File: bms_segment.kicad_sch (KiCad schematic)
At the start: 103 parts, among them J1 Conn_02x09_Counter_Clockwise, J2 Conn_02x09_Counter_Clockwise, J5 Conn_01x04, J6 Conn_01x04, J7 Conn_01x06, SW1 SW_Push, U1 LMR516xx, U2 MAX14921, U3 ADuM1252, U4 STM32F103C8Tx, U5 MAX11163, U6 REF61xx

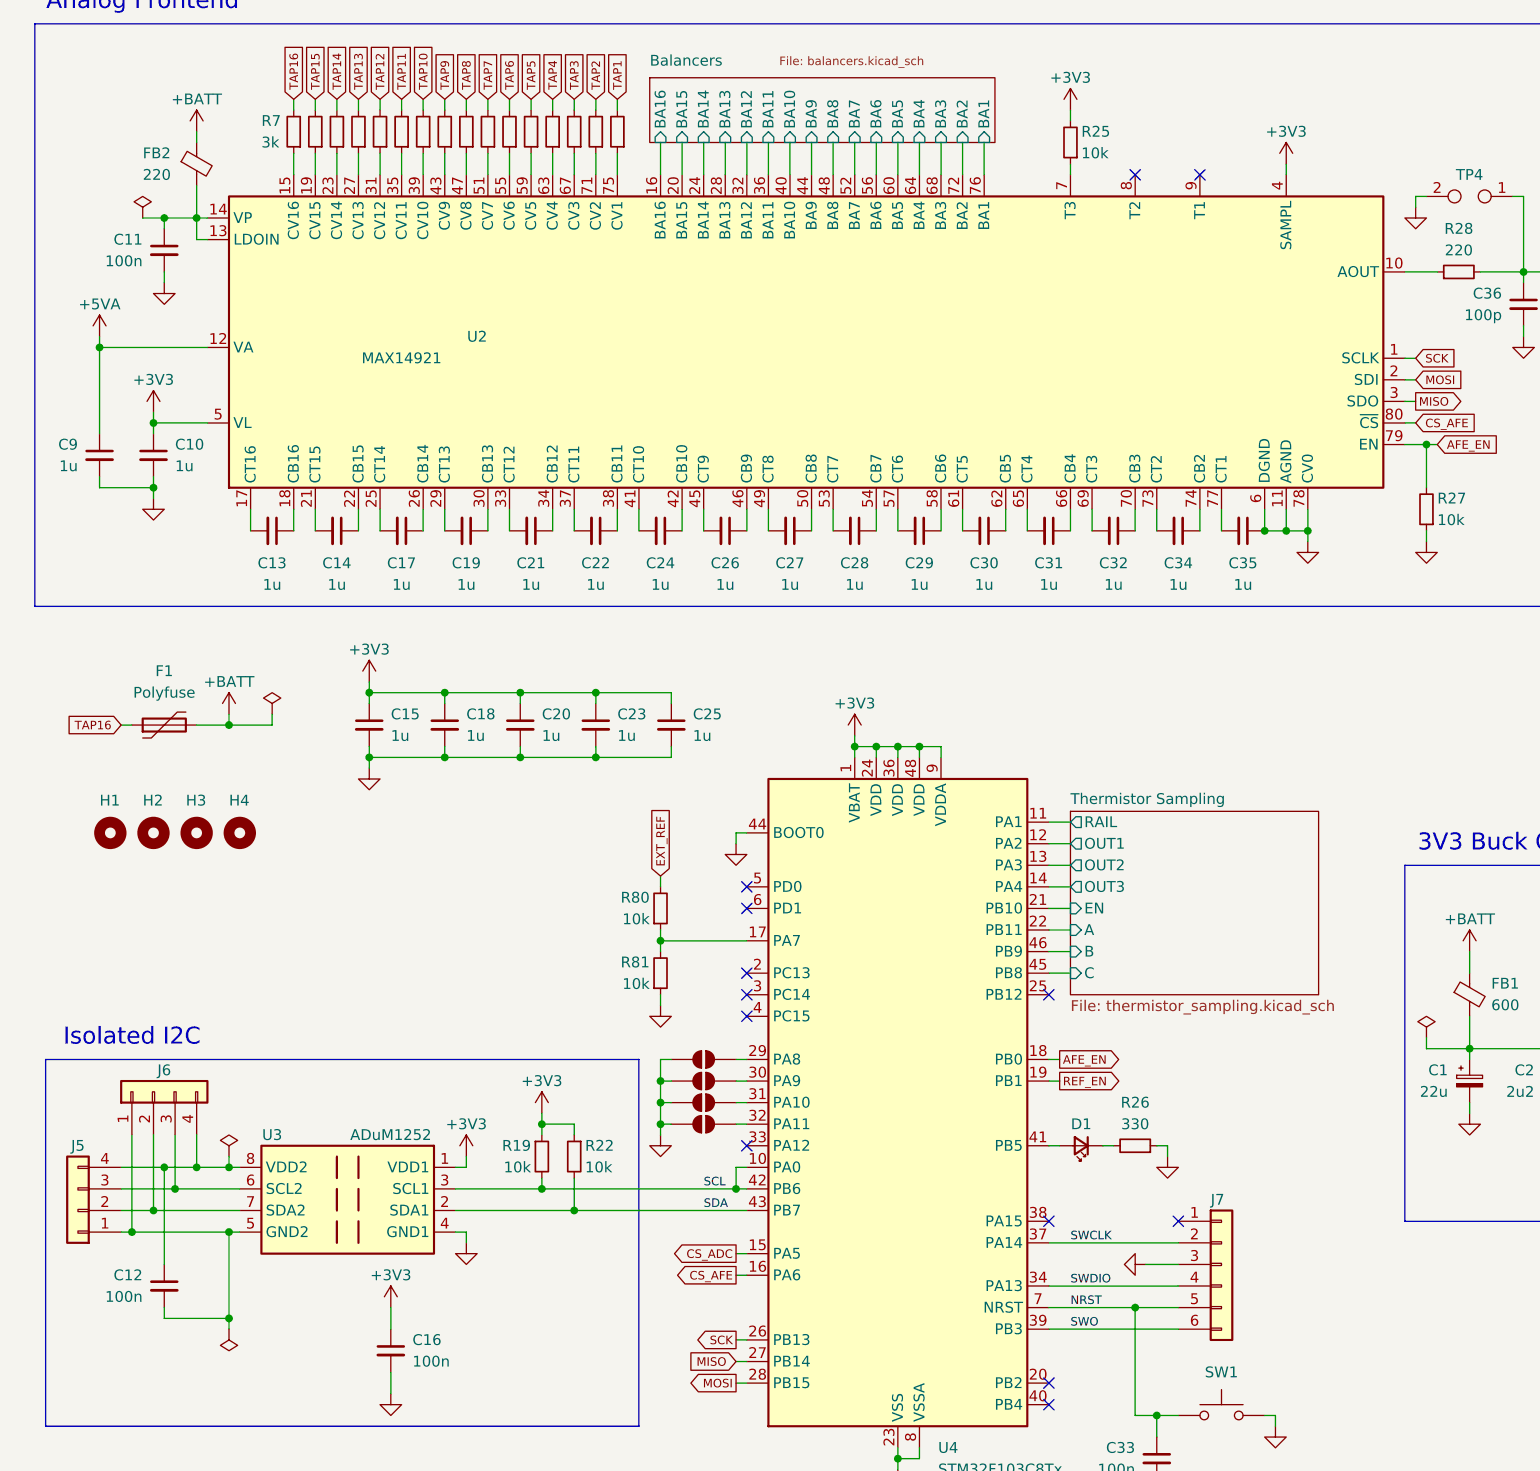
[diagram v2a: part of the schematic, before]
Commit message: schematic: Fix I2C connector pin order
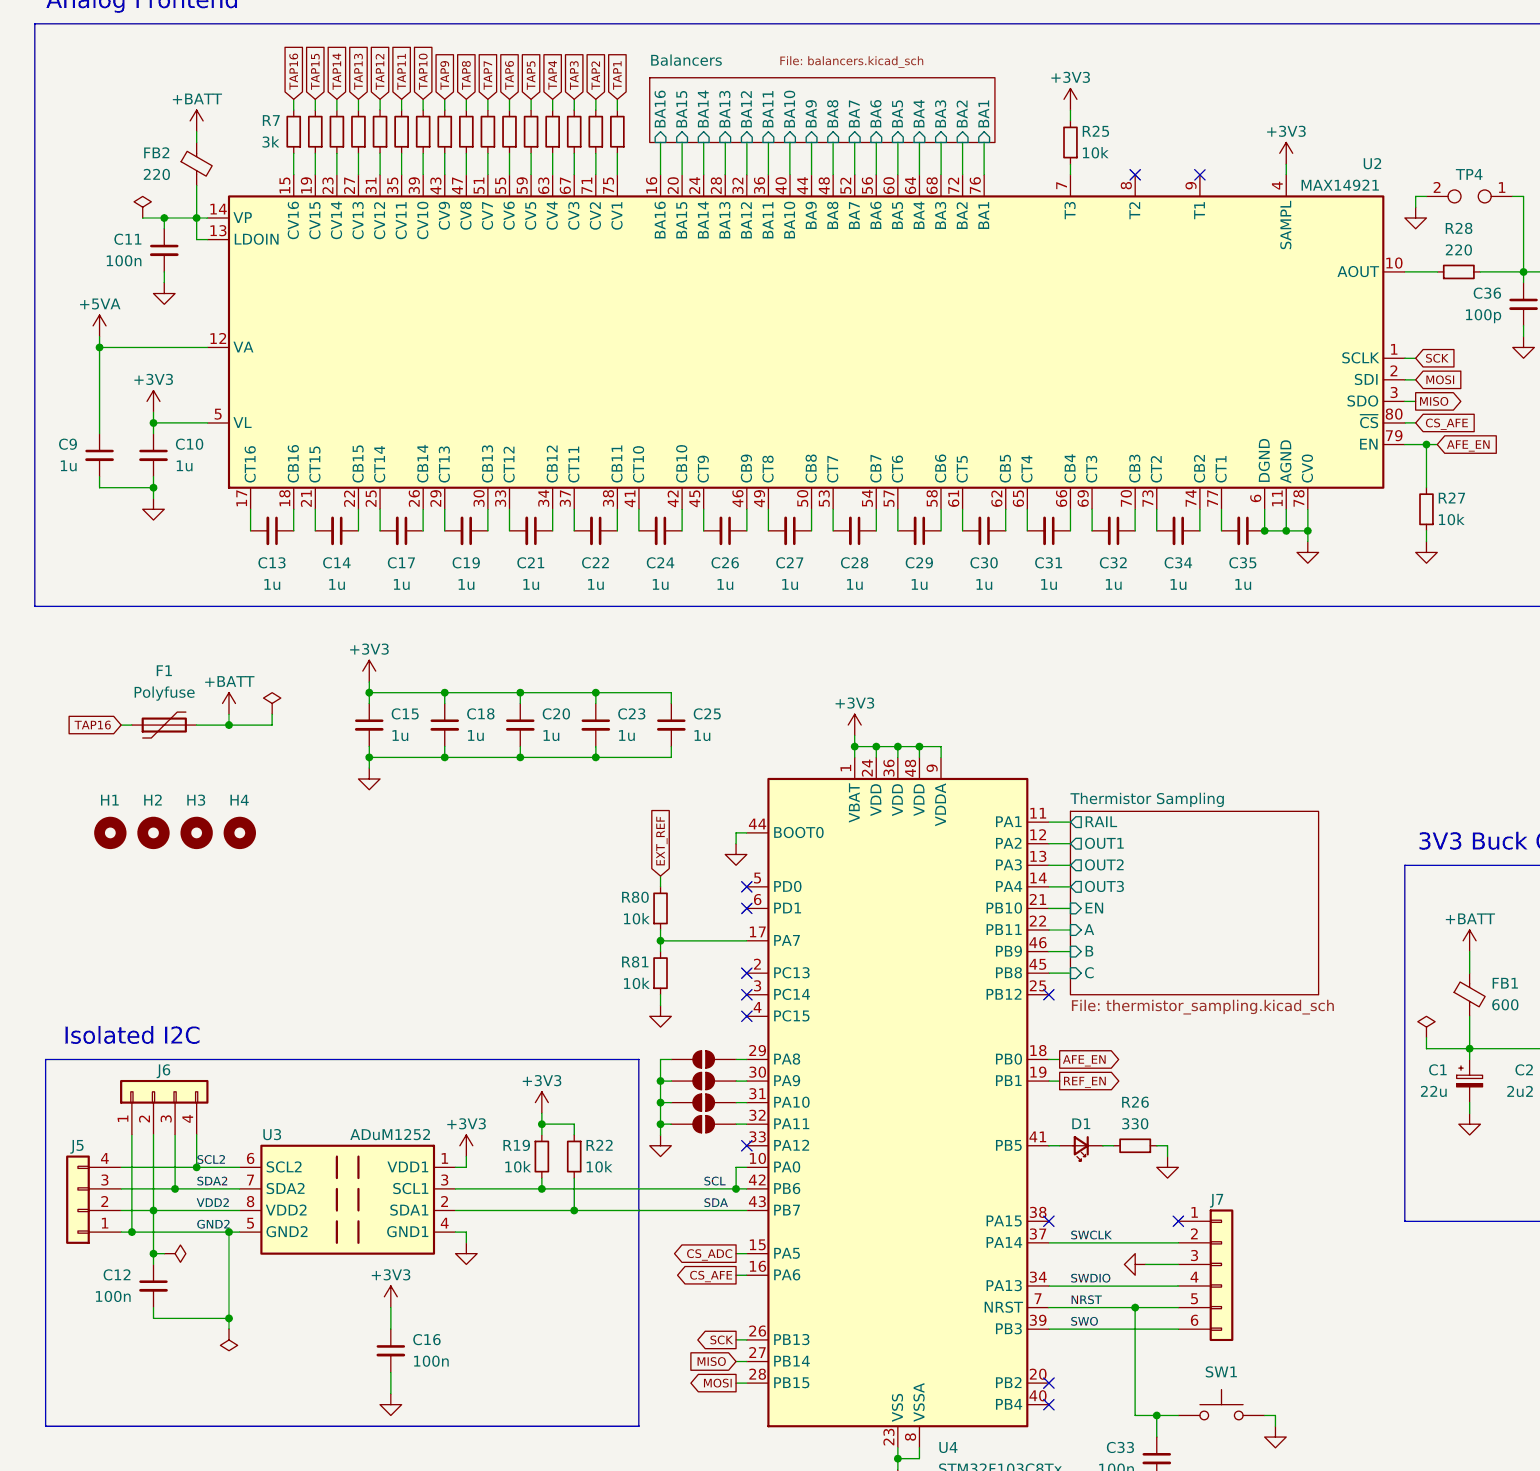
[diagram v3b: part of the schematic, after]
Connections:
- net GND2: now reaches C12.2, J5.1 (Pin_1), J6.1 (Pin_1), U3.5 (GND2)
- net SDA2: now reaches J5.3 (Pin_3), J6.3 (Pin_3)
- net SDA2: now also U3.7 (SDA2); no longer U3.6 (SCL2)
- net VDD2: now reaches J5.2 (Pin_2), J6.2 (Pin_2)
- net VDD2: now also C12.1, U3.8 (VDD2); no longer U3.7 (SDA2)
- net SCL2: now reaches J5.4 (Pin_4), J6.4 (Pin_4)
- net SCL2: now also U3.6 (SCL2); no longer C12.1, U3.8 (VDD2)
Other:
- moved on the sheet: C12
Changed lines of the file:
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@@
 	)
 	(junction
-		(at 30.48 153.67)
-		(diameter 0)
-		(color 0 0 0 0)
-	)
-	(junction
 		(at 74.93 148.59)
 		(diameter 0)
@@
 	)
 	(junction
-		(at 38.1 153.67)
-		(diameter 0)
-		(color 0 0 0 0)
-	)
-	(junction
 		(at 236.22 53.34)
 		(diameter 0)
@@
 	)
 	(junction
+		(at 29.21 163.83)
+		(diameter 0)
+		(color 0 0 0 0)
+	)
+	(junction
 		(at 240.03 29.21)
 		(diameter 0)
@@
 	(wire
 		(pts
-			(xy 29.21 158.75) (xy 39.37 158.75)
-		)
-		(stroke
-			(width 0)
-			(type default)
-		)
-	)
-	(wire
-		(pts
 			(xy 96.52 33.02) (xy 96.52 36.83)
 		)
@@
 	(wire
 		(pts
-			(xy 30.48 171.45) (xy 30.48 170.18)
-		)
-		(stroke
-			(width 0)
-			(type default)
-		)
-	)
-	(wire
-		(pts
-			(xy 25.4 153.67) (xy 30.48 153.67)
+			(xy 29.21 171.45) (xy 29.21 170.18)
 		)
 		(stroke
@@
 	(wire
 		(pts
+			(xy 29.21 158.75) (xy 39.37 158.75)
+		)
+		(stroke
+			(width 0)
+			(type default)
+		)
+	)
+	(wire
+		(pts
 			(xy 231.14 93.98) (xy 232.41 93.98)
 		)
@@
 	(wire
 		(pts
+			(xy 29.21 163.83) (xy 29.21 165.1)
+		)
+		(stroke
+			(width 0)
+			(type default)
+		)
+	)
+	(wire
+		(pts
 			(xy 231.14 99.06) (xy 231.14 101.6)
 		)
@@
 	(wire
 		(pts
+			(xy 29.21 163.83) (xy 30.48 163.83)
+		)
+		(stroke
+			(width 0)
+			(type default)
+		)
+	)
+	(wire
+		(pts
 			(xy 63.5 27.94) (xy 63.5 29.21)
 		)
@@
 	(wire
 		(pts
-			(xy 30.48 153.67) (xy 30.48 165.1)
-		)
-		(stroke
-			(width 0)
-			(type default)
-		)
-	)
-	(wire
-		(pts
 			(xy 255.27 147.32) (xy 255.27 148.59)
 		)
@@
 	(wire
 		(pts
-			(xy 38.1 153.67) (xy 39.37 153.67)
-		)
-		(stroke
-			(width 0)
-			(type default)
-		)
-	)
-	(wire
-		(pts
-			(xy 34.29 153.67) (xy 38.1 153.67)
+			(xy 34.29 153.67) (xy 39.37 153.67)
 		)
 		(stroke
@@
 	(wire
 		(pts
-			(xy 38.1 152.4) (xy 38.1 153.67)
-		)
-		(stroke
-			(width 0)
-			(type default)
-		)
-	)
-	(wire
-		(pts
 			(xy 261.62 101.6) (xy 262.89 101.6)
 		)
@@
 	(wire
 		(pts
-			(xy 30.48 153.67) (xy 34.29 153.67)
+			(xy 25.4 153.67) (xy 34.29 153.67)
 		)
 		(stroke
@@
 	(wire
 		(pts
-			(xy 30.48 171.45) (xy 38.1 171.45)
+			(xy 29.21 171.45) (xy 38.1 171.45)
 		)
 		(stroke
@@
 	(wire
 		(pts
+			(xy 29.21 158.75) (xy 29.21 163.83)
+		)
+		(stroke
+			(width 0)
+			(type default)
+		)
+	)
+	(wire
+		(pts
 			(xy 238.76 31.75) (xy 241.3 31.75)
 		)
@@
 		)
 	)
+	(label "GND2"
+		(at 34.29 161.29 0)
+		(effects
+			(font
+				(size 1 1)
+			)
+			(justify left bottom)
+		)
+	)
 	(label "NRST"
 		(at 137.16 170.18 0)
@@
 		)
 	)
+	(label "VDD2"
+		(at 34.29 158.75 0)
+		(effects
+			(font
+				(size 1 1)
+			)
+			(justify left bottom)
+		)
+	)
+	(label "SCL2"
+		(at 34.29 153.67 0)
+		(effects
+			(font
+				(size 1 1)
+			)
+			(justify left bottom)
+		)
+	)
+	(label "SDA2"
+		(at 34.29 156.21 0)
+		(effects
+			(font
+				(size 1 1)
+			)
+			(justify left bottom)
+		)
+	)
 	(label "SWO"
 		(at 137.16 172.72 0)
@@
 		(dnp no)
 		(property "Reference" "U2"
-			(at 67.31 55.88 90)
+			(at 172.72 35.56 90)
 			(effects
 				(font
@@
 		)
 		(property "Value" "MAX14921"
-			(at 58.42 58.42 90)
+			(at 168.91 38.1 90)
 			(effects
 				(font
@@
 	(symbol
 		(lib_id "Device:C_Small")
-		(at 30.48 167.64 0)
+		(at 29.21 167.64 0)
 		(mirror y)
 		(unit 1)
@@
 		(dnp no)
 		(property "Reference" "C12"
-			(at 27.94 166.3762 0)
+			(at 26.67 166.3762 0)
 			(effects
 				(font
@@
 		)
 		(property "Value" "100n"
-			(at 27.94 168.9162 0)
+			(at 26.67 168.9162 0)
 			(effects
 				(font
@@
 		)
 		(property "Footprint" "Capacitor_SMD:C_0603_1608Metric"
-			(at 30.48 167.64 0)
+			(at 29.21 167.64 0)
 			(effects
 				(font
@@
 		)
 		(property "Datasheet" "~"
-			(at 30.48 167.64 0)
+			(at 29.21 167.64 0)
 			(effects
 				(font
@@
 		)
 		(property "Description" "Unpolarized capacitor, small symbol"
-			(at 30.48 167.64 0)
+			(at 29.21 167.64 0)
 			(effects
 				(font
@@
 		)
 		(property "Dist #" "C1591"
-			(at 30.48 167.64 0)
+			(at 29.21 167.64 0)
 			(effects
 				(font
@@
 		)
 		(property "Mfr" "Samsung"
-			(at 30.48 167.64 0)
+			(at 29.21 167.64 0)
 			(effects
 				(font
@@
 		)
 		(property "Mfr #" "CL10B104KB8NNNC"
-			(at 30.48 167.64 0)
+			(at 29.21 167.64 0)
 			(effects
 				(font
@@
 		)
 		(property "Dist" "LCSC"
-			(at 30.48 167.64 0)
+			(at 29.21 167.64 0)
 			(effects
 				(font
@@
 	(symbol
 		(lib_id "power:PWR_FLAG")
-		(at 38.1 152.4 0)
+		(at 30.48 163.83 270)
 		(unit 1)
 		(exclude_from_sim no)
@@
 		(fields_autoplaced yes)
 		(property "Reference" "#FLG03"
-			(at 38.1 150.495 0)
+			(at 32.385 163.83 0)
 			(effects
 				(font
@@
 		)
 		(property "Value" "PWR_FLAG"
-			(at 38.1 147.32 0)
+			(at 35.56 163.83 0)
 			(effects
 				(font
@@
 		)
 		(property "Footprint" ""
-			(at 38.1 152.4 0)
+			(at 30.48 163.83 0)
 			(effects
 				(font
@@
 		)
 		(property "Datasheet" "~"
-			(at 38.1 152.4 0)
+			(at 30.48 163.83 0)
 			(effects
 				(font
@@
 		)
 		(property "Description" "Special symbol for telling ERC where power comes from"
-			(at 38.1 152.4 0)
+			(at 30.48 163.83 0)
 			(effects
 				(font

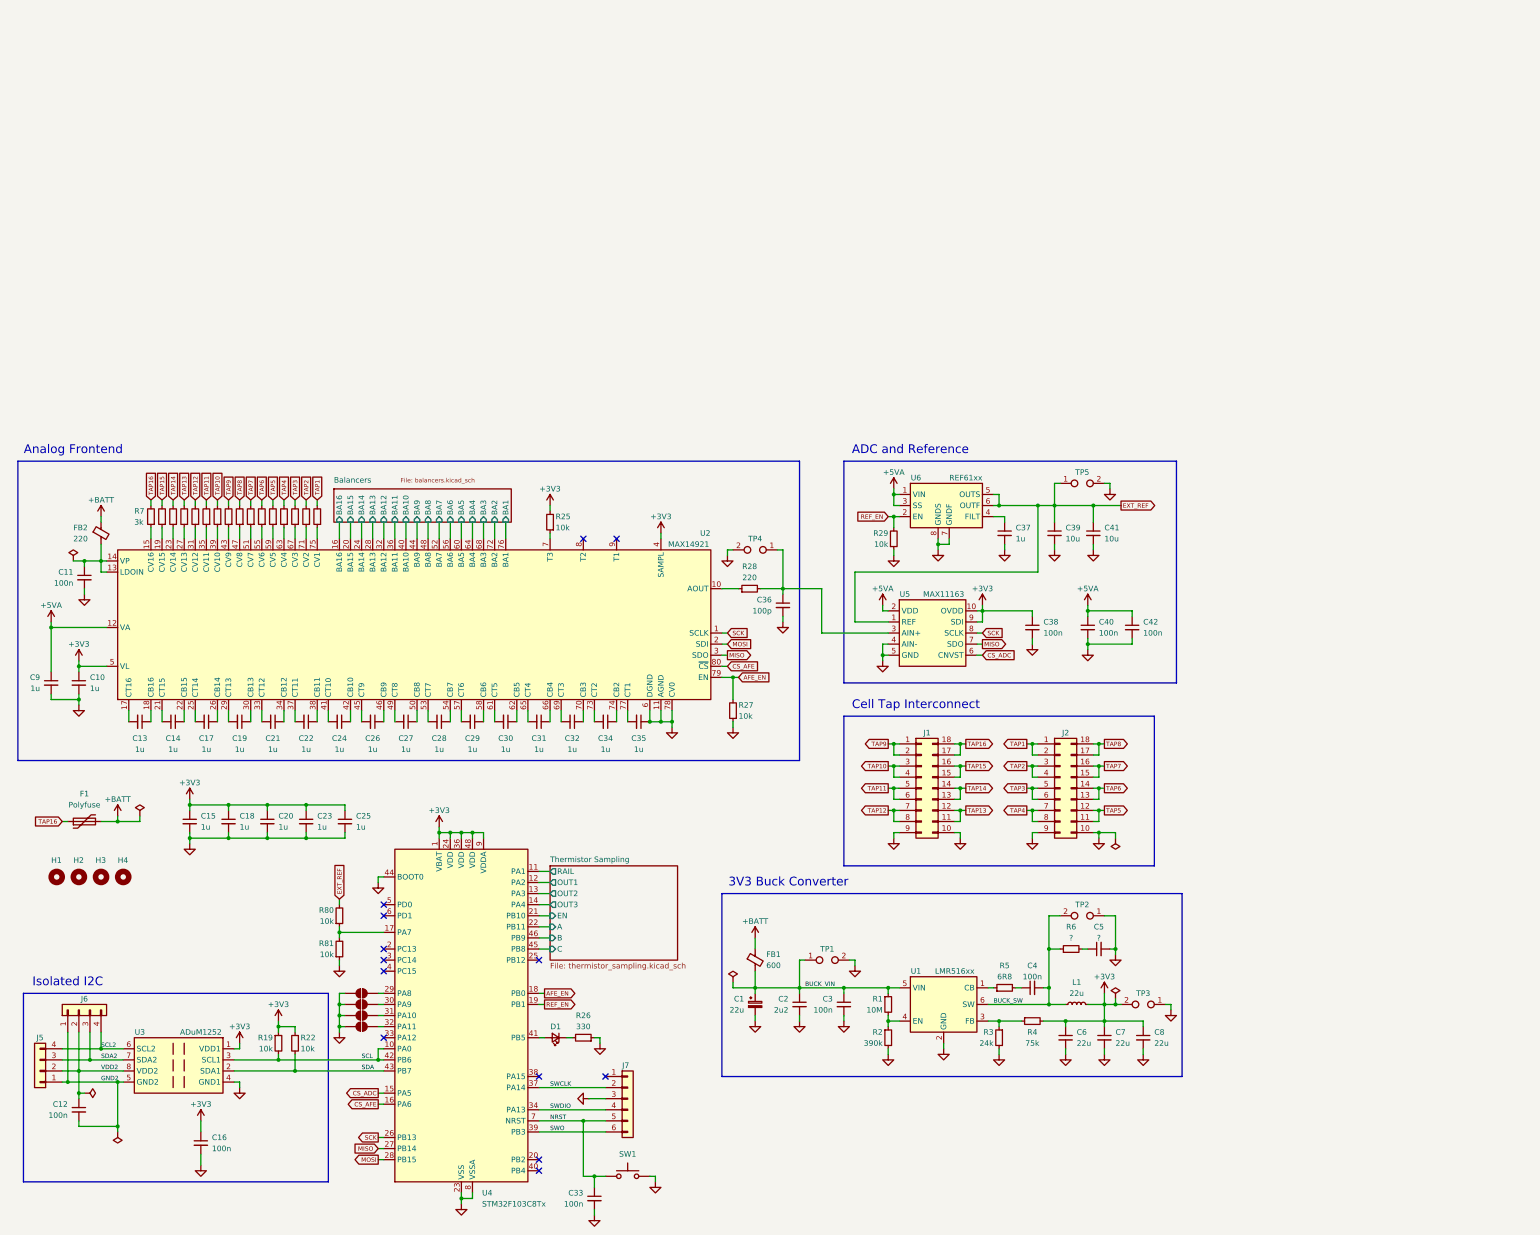
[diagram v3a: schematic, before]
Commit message: schematic: Fix-up reference designators
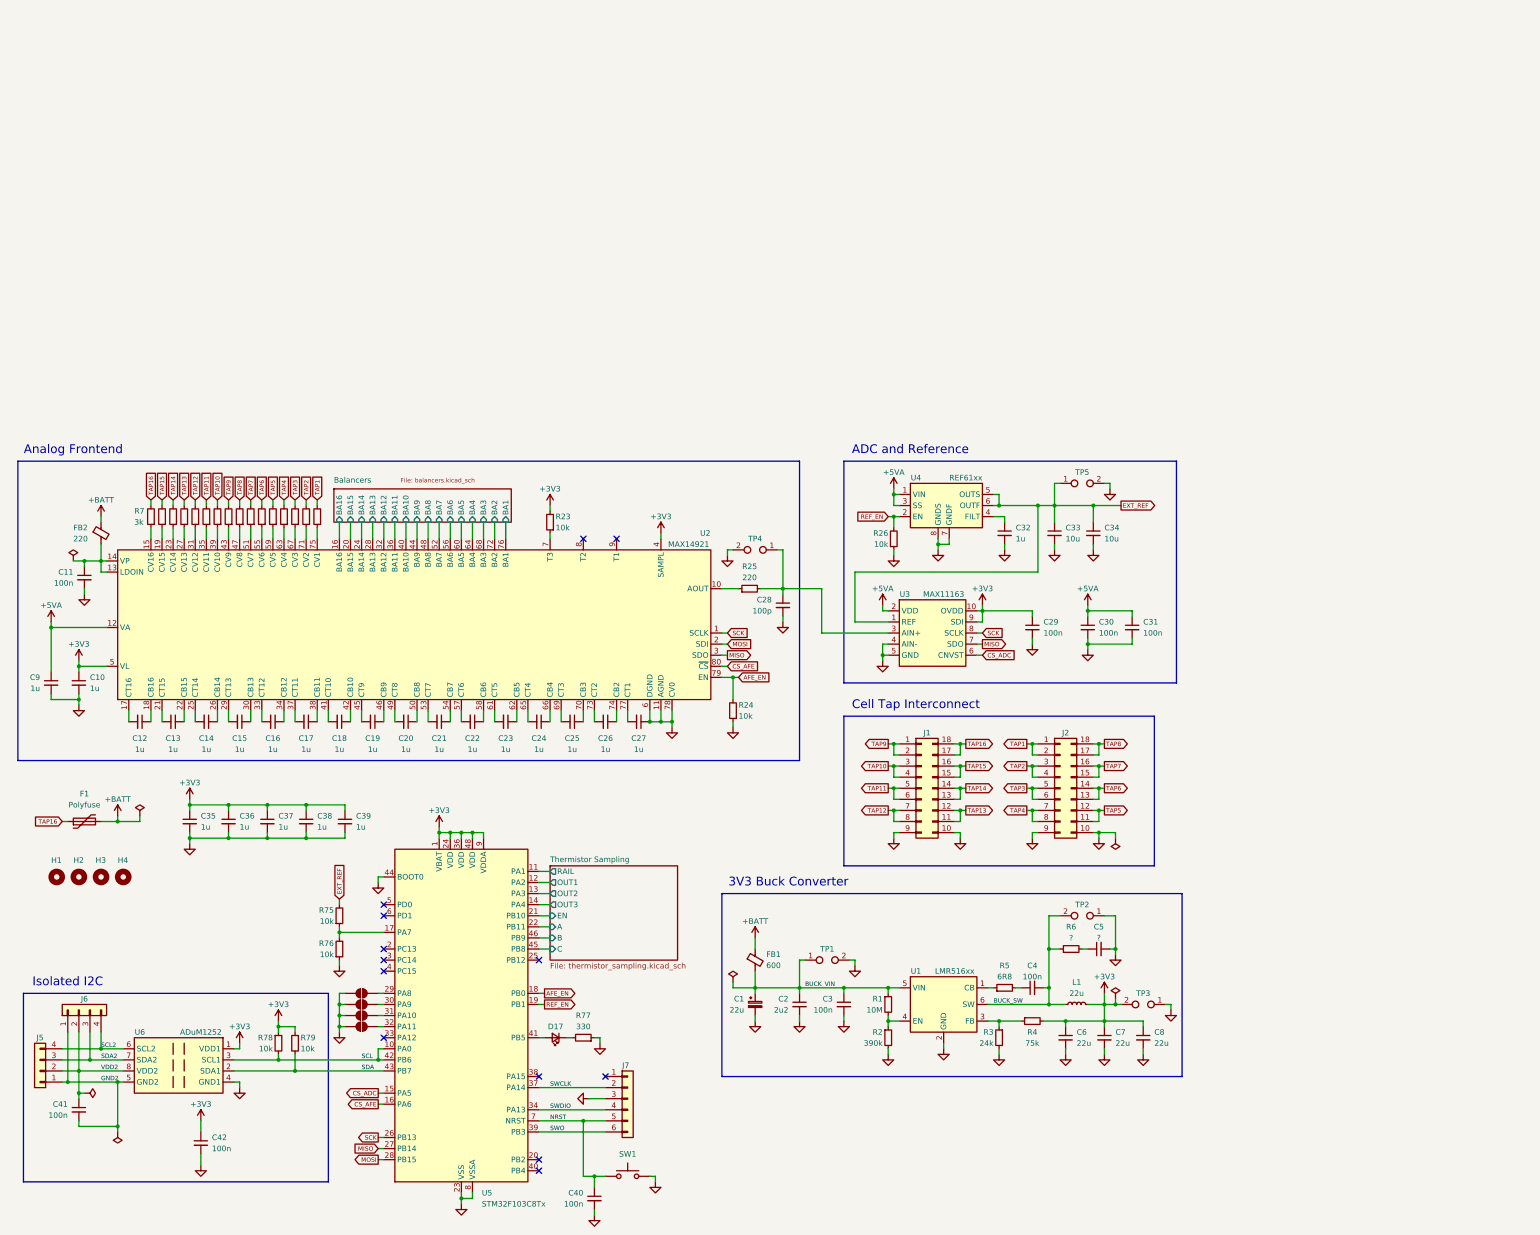
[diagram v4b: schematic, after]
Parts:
- renumbered C13 to C12, C14 to C13, C17 to C14, C19 to C15, C21 to C16, C22 to C17, C24 to C18, C26 to C19, C27 to C20, C28 to C21, C29 to C22, C30 to C23, C31 to C24, C32 to C25, C34 to C26, C35 to C27, C36 to C28, C38 to C29, C40 to C30, C42 to C31, C37 to C32, C39 to C33, C41 to C34, C15 to C35, C18 to C36, C20 to C37, C23 to C38, C25 to C39, C33 to C40, C12 to C41, C16 to C42, D1 to D17, R20 to R19, R21 to R20, R23 to R21, R24 to R22, R25 to R23, R27 to R24, R28 to R25, R29 to R26, R80 to R75, R81 to R76, R26 to R77, R19 to R78, R22 to R79, U5 to U3, U6 to U4, U4 to U5, U3 to U6
